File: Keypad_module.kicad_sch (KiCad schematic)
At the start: 61 parts, among them SW1 SW_Push, SW10 SW_Push, SW11 SW_Push, SW12 SW_Push, SW13 SW_Push, SW14 SW_Push, SW15 SW_Push, SW16 SW_Push, SW17 SW_Push, SW18 SW_Push, SW19 SW_Push, SW2 SW_Push, SW20 SW_Push, SW3 SW_Push, SW4 SW_Push, SW5 SW_Push, SW6 SW_Push, SW7 SW_Push, SW8 SW_Push, SW9 SW_Push, U1 XIAO-nRF52840-SMD, U2 MCP23017_ML

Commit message: Schematic checkpoint before I mess up the layout
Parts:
- removed TP3, TP4, TP5, TP6, TP7, TP8: TestPoint, TestPoint:TestPoint_Pad_D2.0mm, symbol Connector:TestPoint
- added J2: Conn_01x06_Pin, Connector_PinHeader_1.00mm:PinHeader_1x06_P1.00mm_Vertical, symbol Connector:Conn_01x06_Pin
- U1: footprint Seeed Studio XIAO Series Library:modified-XIAO-nRF52840-SMD -> a:modified-XIAO-nRF52840-SMD
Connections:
- net GND: now also J2.6 (Pin_6)
- net K3V3: now also J2.1 (Pin_1)
- net KCOM: now also J2.4 (Pin_4)
- net KPRESENCE: now also J2.3 (Pin_3)
- net KSCL: now also J2.5 (Pin_5)
- net KSDA: now also J2.2 (Pin_2)
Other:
- moved on the sheet: D1, D10, D11, D12, D13, D14, D15, D16, D17, D18, D19, D2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

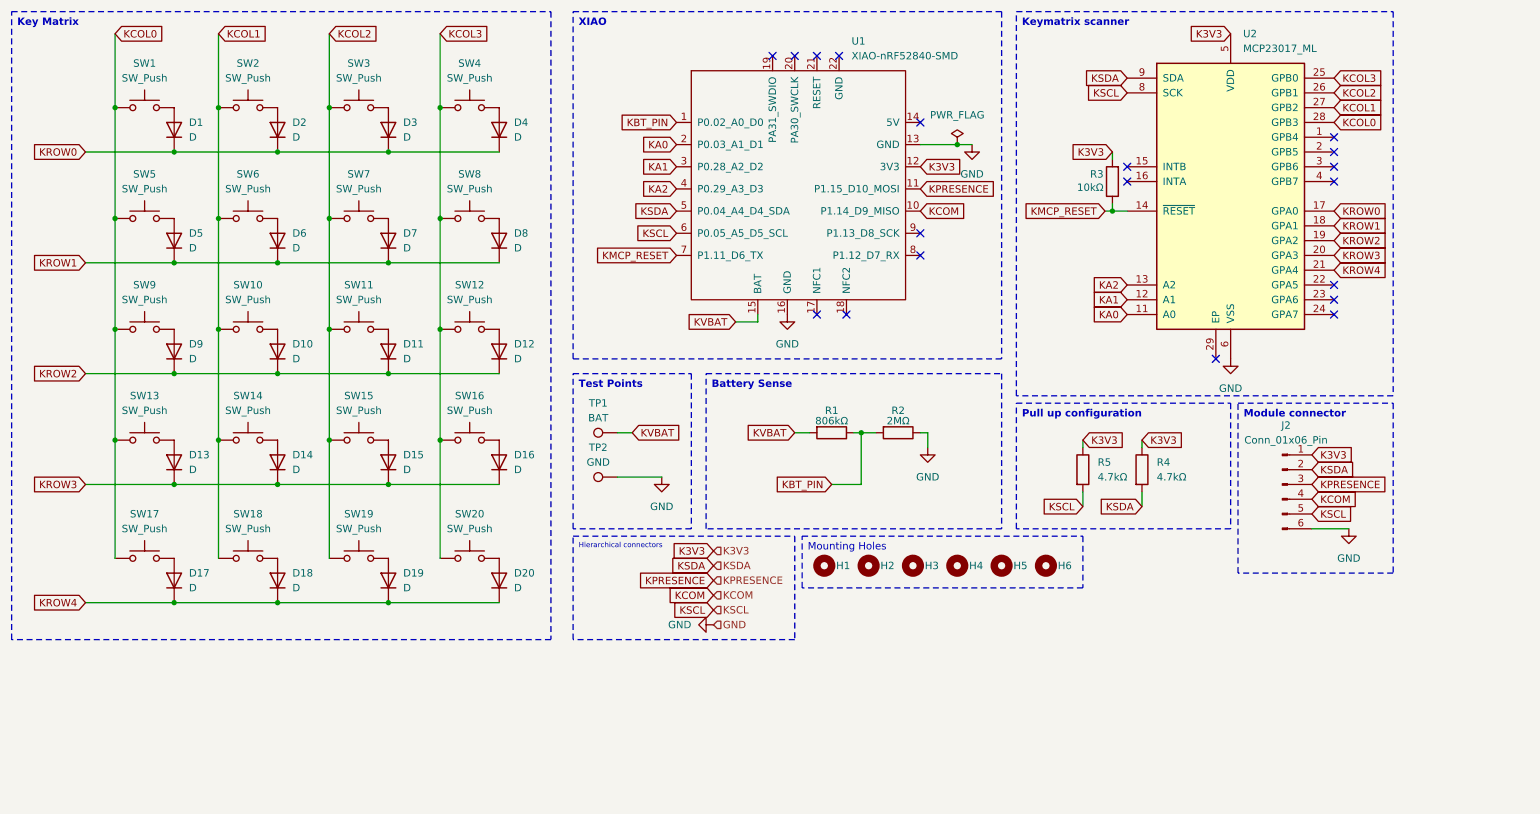
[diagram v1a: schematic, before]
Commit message: I gave up on the hotswao modularity thing
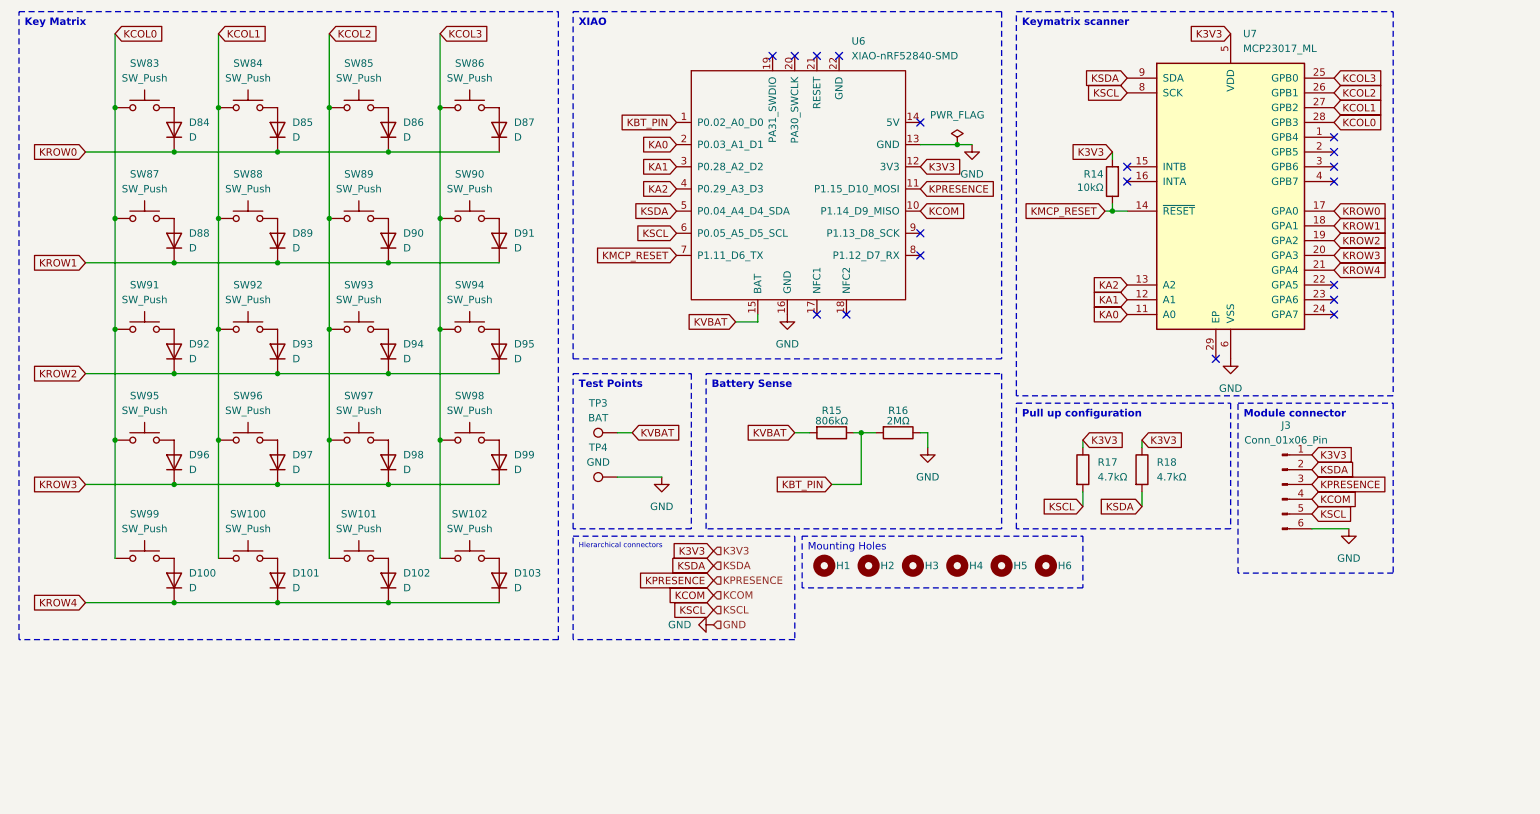
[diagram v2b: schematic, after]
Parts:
- renumbered D17 to D100, D18 to D101, D19 to D102, D20 to D103, D1 to D84, D2 to D85, D3 to D86, D4 to D87, D5 to D88, D6 to D89, D7 to D90, D8 to D91, D9 to D92, D10 to D93, D11 to D94, D12 to D95, D13 to D96, D14 to D97, D15 to D98, D16 to D99, J2 to J3, R3 to R14, R1 to R15, R2 to R16, R5 to R17, R4 to R18, SW18 to SW100, SW19 to SW101, SW20 to SW102, SW1 to SW83, SW2 to SW84, SW3 to SW85, SW4 to SW86, SW5 to SW87, SW6 to SW88, SW7 to SW89, SW8 to SW90, SW9 to SW91, SW10 to SW92, SW11 to SW93, SW12 to SW94, SW13 to SW95, SW14 to SW96, SW15 to SW97, SW16 to SW98, SW17 to SW99, TP1 to TP3, TP2 to TP4, U1 to U6, U2 to U7

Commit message: Finished the main board's design
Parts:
- removed H1, H2, H3, H4, H5, H6: MountingHole, MountingHole:MountingHole_2.2mm_M2, symbol Mechanical:MountingHole
- D100, D101, D102, D103, D84, D85, D86, D87, D88, D89, D90, D91, D92, D93, D94, D95, D96, D97, D98, D99, J3, R14, R15, R16, R17, R18, SW100, SW101, SW102, SW83, SW84, SW85, SW86, SW87, SW88, SW89, SW90, SW91, SW92, SW93, SW94, SW95, SW96, SW97, SW98, SW99, TP3, TP4, U6, U7: now not fitted; now left out of the parts list
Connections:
- net GND: now also U7.11 (A0), U7.12 (A1), U7.13 (A2)
- net K3V3: no longer U7.5 (VDD)
- net KCOL0: now also U7.25 (GPB0); no longer U7.28 (GPB3)
- net KCOL1: now also U7.26 (GPB1); no longer U7.27 (GPB2)
- net KCOL2: now also U7.27 (GPB2); no longer U7.26 (GPB1)
- net KCOL3: now also U7.28 (GPB3); no longer U7.25 (GPB0)
- net KROW0: now also U7.21 (GPA4); no longer U7.17 (GPA0)
- net KROW1: now also U7.20 (GPA3); no longer U7.18 (GPA1)
- net KROW3: now also U7.18 (GPA1); no longer U7.20 (GPA3)
- net KROW4: now also U7.17 (GPA0); no longer U7.21 (GPA4)
- net K5V: now reaches U6.14 (5V)
- net KA0: no longer names the net of U6.2 (P0.03_A1_D1)
- net KA0: no longer U7.11 (A0)
- net KA1: no longer names the net of U6.3 (P0.28_A2_D2)
- net KA1: no longer U7.12 (A1)
- net KA2: no longer names the net of U6.4 (P0.29_A3_D3)
- net KA2: no longer U7.13 (A2)
- no-connect marks 19 -> 26

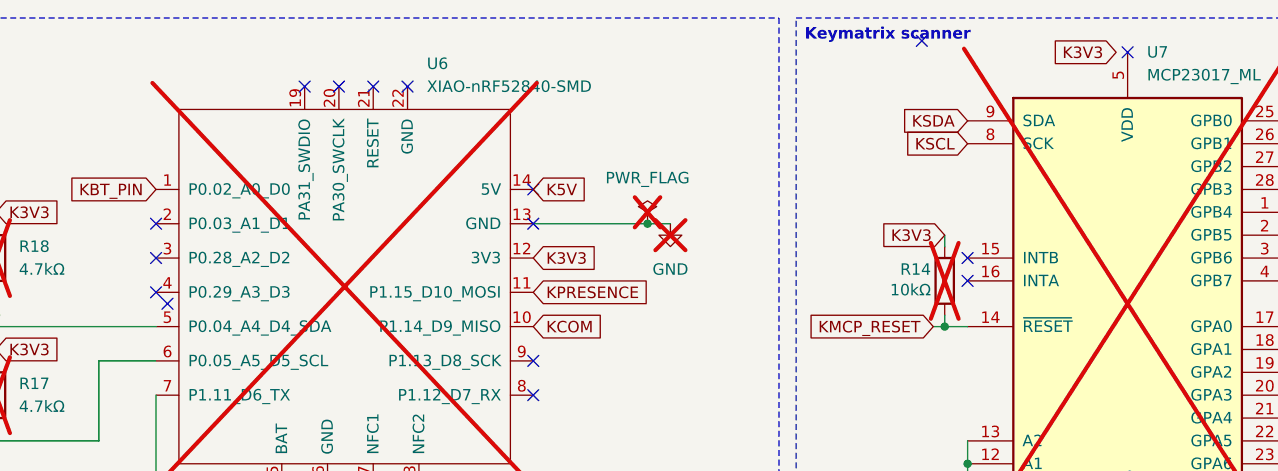
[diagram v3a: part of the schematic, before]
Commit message: Reduced the main keyboard's profile
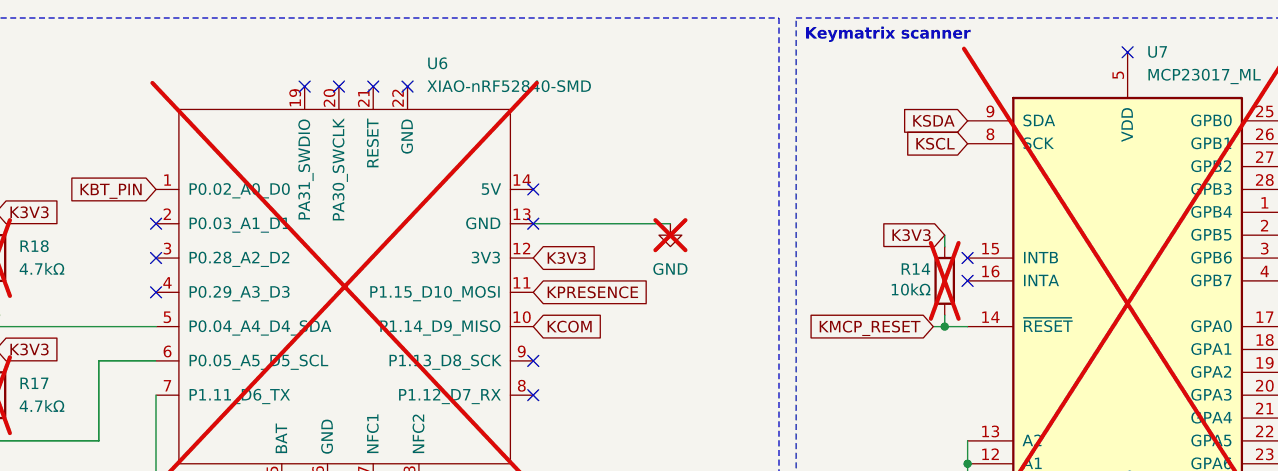
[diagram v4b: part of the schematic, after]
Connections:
- net K5V: no longer names the net of U6.14 (5V)
- no-connect marks 26 -> 24
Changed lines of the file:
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@@
 	)
 	(junction
-		(at 194.31 38.1)
-		(diameter 0)
-		(color 0 0 0 0)
-	)
-	(junction
 		(at 227.33 49.53)
 		(diameter 0)
@@
 	)
 	(no_connect
-		(at 140.97 46.99)
-	)
-	(no_connect
 		(at 265.43 39.37)
 	)
@@
 	)
 	(no_connect
-		(at 224.79 17.78)
-	)
-	(no_connect
 		(at 163.83 22.86)
 	)
@@
 	(wire
 		(pts
-			(xy 196.85 38.1) (xy 194.31 38.1)
+			(xy 181.61 38.1) (xy 196.85 38.1)
 		)
 		(stroke
@@
 	(wire
 		(pts
-			(xy 181.61 38.1) (xy 194.31 38.1)
-		)
-		(stroke
-			(width 0)
-			(type default)
-		)
-	)
-	(wire
-		(pts
 			(xy 60.96 58.42) (xy 80.01 58.42)
 		)
@@
 		)
 	)
-	(global_label "K5V"
-		(shape input)
-		(at 181.61 34.29 0)
-		(fields_autoplaced yes)
-		(effects
-			(font
-				(size 1.27 1.27)
-			)
-			(justify left)
-		)
-		(property "Intersheetrefs" "${INTERSHEET_REFS}"
-			(at 188.1633 34.29 0)
-			(effects
-				(font
-					(size 1.27 1.27)
-				)
-				(justify left)
-				(hide yes)
-			)
-		)
-	)
 	(global_label "KBT_PIN"
 		(shape input)
@@
 		)
 	)
-	(global_label "K3V3"
-		(shape input)
-		(at 246.38 19.05 180)
-		(fields_autoplaced yes)
-		(effects
-			(font
-				(size 1.27 1.27)
-			)
-			(justify right)
-		)
-		(property "Intersheetrefs" "${INTERSHEET_REFS}"
-			(at 238.6172 19.05 0)
-			(effects
-				(font
-					(size 1.27 1.27)
-				)
-				(justify right)
-				(hide yes)
-			)
-		)
-	)
 	(global_label "KSCL"
 		(shape input)
@@
 					(unit 1)
 				)
-			)
-		)
-	)
-	(symbol
-		(lib_id "power:PWR_FLAG")
-		(at 194.31 38.1 0)
-		(unit 1)
-		(exclude_from_sim yes)
-		(in_bom no)
-		(on_board no)
-		(dnp yes)
-		(fields_autoplaced yes)
-		(property "Reference" "#FLG03"
-			(at 194.31 36.195 0)
-			(effects
-				(font
-					(size 1.27 1.27)
-				)
-				(hide yes)
-			)
-		)
-		(property "Value" "PWR_FLAG"
-			(at 194.31 33.02 0)
-			(effects
-				(font
-					(size 1.27 1.27)
-				)
-			)
-		)
-		(property "Footprint" ""
-			(at 194.31 38.1 0)
-			(effects
-				(font
-					(size 1.27 1.27)
-				)
-				(hide yes)
-			)
-		)
-		(property "Datasheet" "~"
-			(at 194.31 38.1 0)
-			(effects
-				(font
-					(size 1.27 1.27)
-				)
-				(hide yes)
-			)
-		)
-		(property "Description" "Special symbol for telling ERC where power comes from"
-			(at 194.31 38.1 0)
-			(effects
-				(font
-					(size 1.27 1.27)
-				)
-				(hide yes)
-			)
-		)
-		(pin "1"
-		)
-		(instances
-			(project ""
-				(path "/fa4d5580-8795-4b64-903a-bec98e134c5c/ce80b2d0-ef32-496a-831b-baf9fb5d3f1d"
-					(reference "#FLG03")
-					(unit 1)
-				)
